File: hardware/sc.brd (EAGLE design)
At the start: 92 x 56 mm, 102 parts, among them K1 RT424F124, K2 RT424F124, Q1 si2305cd, Q2 8MHz, Q3 si2305cd, Q4 si2305cd, Q5 si2305cd, Q7 si2305cd, T1 BC846, T2 BC846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

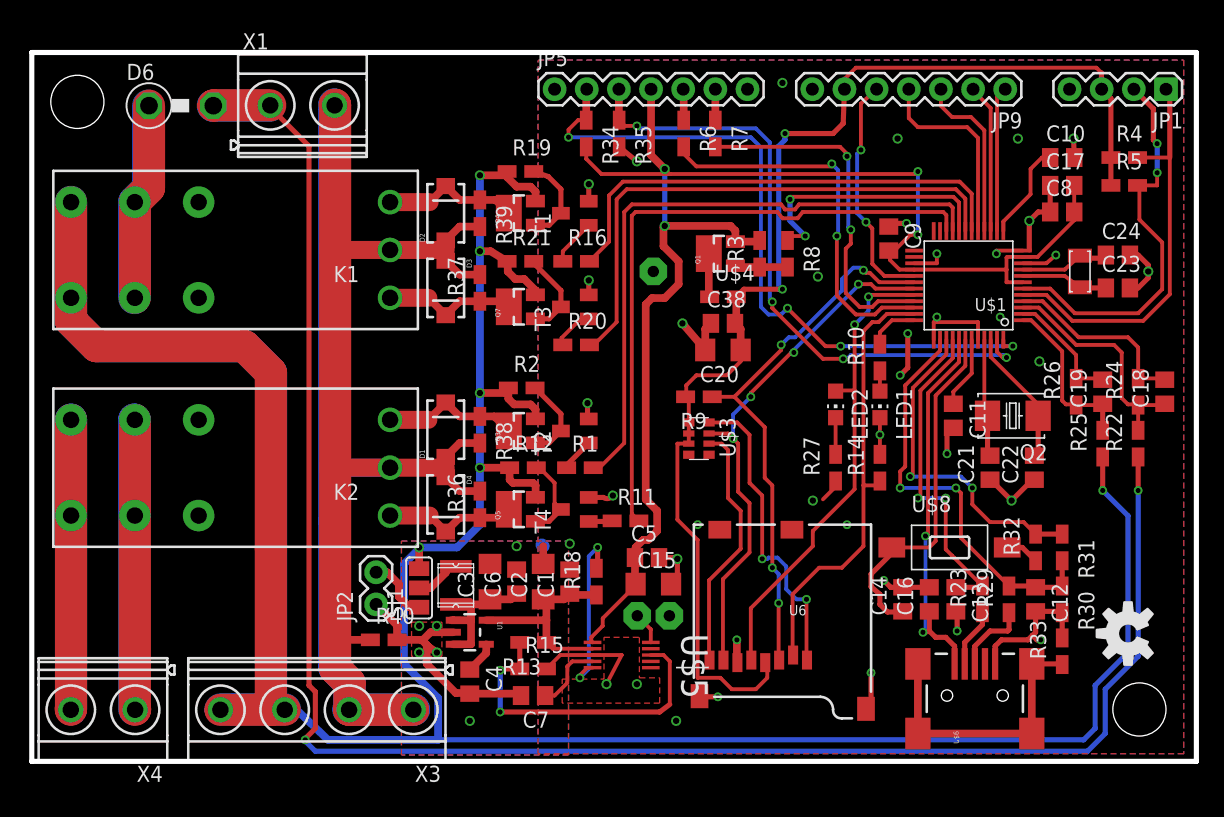
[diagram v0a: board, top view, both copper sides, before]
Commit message: calculate resistor dividers and XT1, XT2 load caps
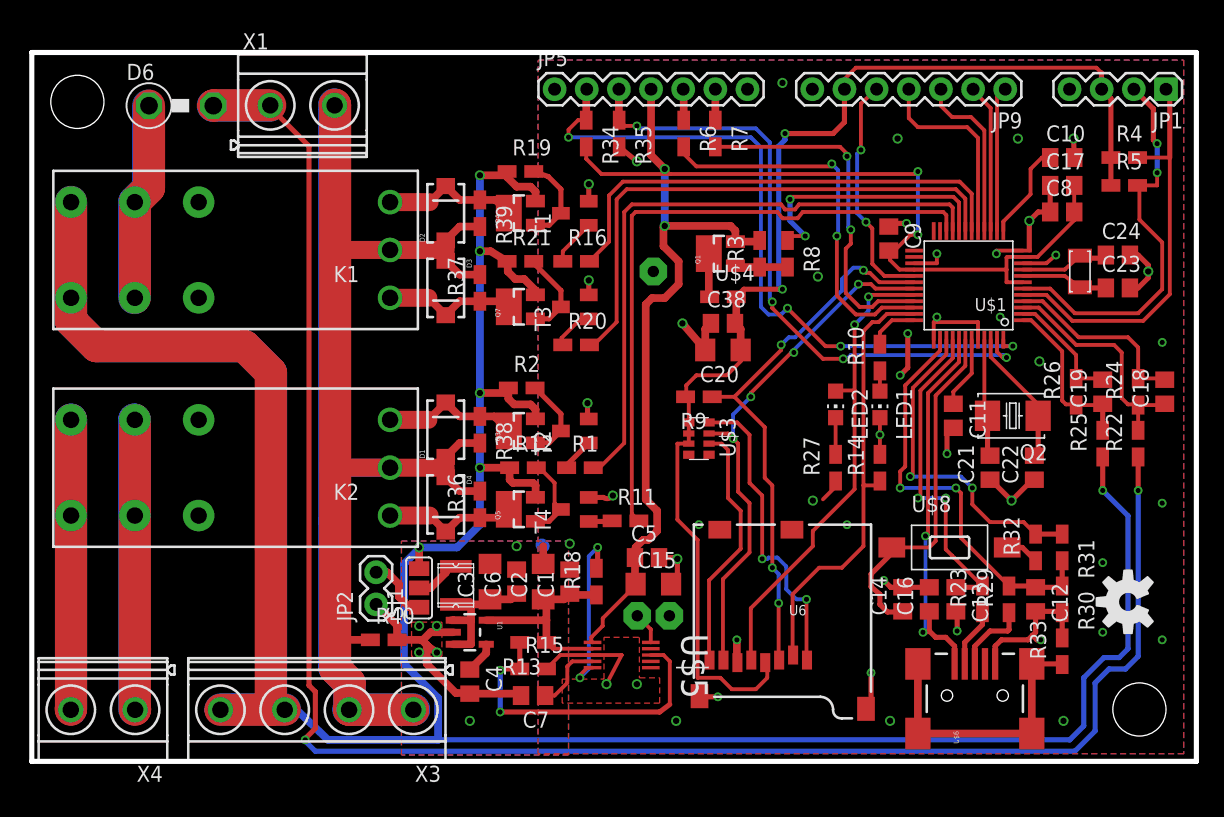
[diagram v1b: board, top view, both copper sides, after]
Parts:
- C13: value 10p -> 10pF
- C14: value 100n -> 100nF
- C18, C19: value 100nF -> 10nF
- C21, C22: value 22p -> 33pF
- C23, C24: value 22p -> 22pF
- C4: value 470pF -> 1uF
- LED2: value green -> orange
- Q2: value 8MHz -> 8MHz 18pF
- R15: value NA -> 56k
- R22, R25: value 100k -> 2M
- R24, R26: value 100k -> 240k
- Y1: value 32768Hz -> 32768Hz CFPX-217 12.5pF
- moved U$7 2.50 mm to (86.6, 12.6)
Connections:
- net VBAT_IN renamed PV+
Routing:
- net GND: vias 43 -> 52
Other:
- board text added: "+"
- board text added: "-"
- board text added: "1.0"
- board text added: "1.1"
- board text added: "1.2"
- board text added: "1.3"
- board text added: "12V bat"
- board text added: "4.0"
- board text added: "debug"
- board text added: "digital"
- board text added: "en"
- board text added: "gnd"
- board text added: "i2c"
- board text added: "opt sw"
- board text added: "photov"
- board text added: "pv+"
- board text added: "pv-"
- board text added: "rst"
- board text added: "rx"
- board text added: "test"
- board text added: "tx"
- board text added: "vcc"

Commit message: use different p-mosfet
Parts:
- Q3, Q4, Q5, Q7: value si2305cd -> IRLML9301
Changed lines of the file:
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@@
 <element name="R9" library="rcl" package="R0805W" value="10k" x="52.7" y="28.8" rot="R180"/>
 <element name="R14" library="rcl" package="R0805W" value="1M" x="67" y="23.2" rot="R90"/>
-<element name="Q4" library="Simplex-DiscreteSemi" package="SOT23-3_POWER" value="si2305cd" x="38.4" y="43.3" rot="R90"/>
+<element name="Q4" library="Simplex-DiscreteSemi" package="SOT23-3_POWER" value="IRLML9301" x="38.4" y="43.3" rot="R90"/>
 <element name="T1" library="transistor" package="SOT23" value="BC846" x="42.9" y="43.3" rot="R90"/>
 <element name="R16" library="rcl" package="R0805W" value="100k" x="43" y="39.5"/>
 <element name="R19" library="rcl" package="R0805W" value="10k" x="38.6" y="46.6"/>
-<element name="Q7" library="Simplex-DiscreteSemi" package="SOT23-3_POWER" value="si2305cd" x="38.4" y="35.9" rot="R90"/>
+<element name="Q7" library="Simplex-DiscreteSemi" package="SOT23-3_POWER" value="IRLML9301" x="38.4" y="35.9" rot="R90"/>
 <element name="T3" library="transistor" package="SOT23" value="BC846" x="42.9" y="35.9" rot="R90"/>
 <element name="R20" library="rcl" package="R0805W" value="100k" x="43" y="32.9"/>
@@
 <attribute name="OC_FARNELL" value="unknown" x="15.7" y="23.2" size="1.778" layer="27" rot="R180" display="off"/>
 </element>
-<element name="Q3" library="Simplex-DiscreteSemi" package="SOT23-3_POWER" value="si2305cd" x="38.4" y="26.1" rot="R90"/>
+<element name="Q3" library="Simplex-DiscreteSemi" package="SOT23-3_POWER" value="IRLML9301" x="38.4" y="26.1" rot="R90"/>
 <element name="T2" library="transistor" package="SOT23" value="BC846" x="42.9" y="26.1" rot="R90"/>
 <element name="R1" library="rcl" package="R0805W" value="100k" x="43.3" y="23.2"/>
 <element name="R2" library="rcl" package="R0805W" value="10k" x="38.7" y="29.5"/>
-<element name="Q5" library="Simplex-DiscreteSemi" package="SOT23-3_POWER" value="si2305cd" x="38.4" y="19.9" rot="R90"/>
+<element name="Q5" library="Simplex-DiscreteSemi" package="SOT23-3_POWER" value="IRLML9301" x="38.4" y="19.9" rot="R90"/>
 <element name="T4" library="transistor" package="SOT23" value="BC846" x="42.9" y="19.9" rot="R90"/>
 <element name="R11" library="rcl" package="R0805W" value="100k" x="46.9" y="19"/>

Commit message: rev3
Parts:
- removed D1, D3, D4: M4, SparkFun-DiscreteSemi:SMA-DIODE
- removed D6: diode, diode:C1702-05
- removed K1, K2: RT424F124, relay:RT424
- removed Q4, Q5, Q7: IRLML9301, Simplex-DiscreteSemi:SOT23-3_POWER
- removed R1: 100k, rcl:R0805W
- removed R37, R38, R39: 470, rcl:R0805W
- removed SJ1: pwr_sel, jumper:SJ_2
- removed T2, T3, T4: BC846, transistor:SOT23
- removed X1, X4: MKDSN1,5/2-5,08, con-phoenix-508:MKDSN1,5/2-5,08
- added C25, C28: 100nF, rcl:C0805
- added C26: 1uF, SparkFun-Capacitors:PANASONIC_D
- added C27: 10uF, SparkFun-Capacitors:PANASONIC_D
- added IC1: PB137ACV, linear:TO220V
- added IC2: INA168, burr-brown:SOT23-5
- added LED3, LED4, LED5, LED6, LED7, LED8: green, led:CHIP-LED0805
- added R17, R28: 1K, rcl:R0805W
- added RL: 150k, rcl:R0805W
- added RS: 0R05, Simplex-rlc:TO220ACS
- D2: value M4 -> SB560; device SparkFun-DiscreteSemi:SMA-DIODE -> diode:C1702-05
- JP2: value bat -> thermistor; device SparkFun:1X02 -> SparkFun-Connectors:1X02
- Q3: value IRLML9301 -> IRFR5305; device Simplex-DiscreteSemi:SOT23-3_POWER -> transistor-power:D-PAK_TO252AA
- R11: value 100k -> 30k
- R12, R21: value 10k -> 1K
- R20: value 100k -> 1K
- R36: value 470 -> 1K
- moved U$7 62.6 mm to (25.1, 24.2), turned to 0 degrees
- moved T1 46.6 mm to (5.30, 15.7), turned to 0 degrees
- moved R19 41.8 mm to (6.30, 20.0), turned to 270 degrees
- moved R2 35.8 mm to (4.20, 20.0), turned to 90 degrees
- moved Q3 33.3 mm to (5.20, 28.5), turned to 0 degrees
- moved JP2 25.8 mm to (1.80, 17.0), turned to 270 degrees
- moved R16 22.1 mm to (34.2, 19.2)
- moved D2 21.4 mm to (14.1, 32.7), turned to 180 degrees
- moved R36 18.7 mm to (34.2, 39.0), turned to 180 degrees
- moved R11 15.5 mm to (41.7, 4.40), turned to 270 degrees
- moved R20 14.5 mm to (34.2, 21.4)
- moved X3 12.1 mm to (10.5, 5.70)
- moved C22 10.0 mm to (70.1, 27.4), turned to 270 degrees
- moved C21 9.84 mm to (66.8, 27.4), turned to 270 degrees
- moved U$2 9.41 mm to (24.1, 14.3)
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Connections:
- removed net CHARGE_OFF: R20.2, U$1.19
- removed net CHARGE_ON: R16.2, U$1.18
- removed net N$31: R20.1, T3.1
- removed net N$32: Q7.1, R21.2, T3.3
- removed net N$33: K2.11, K2.21, X4.1
- removed net N$35: D3.C, K1.A2, Q7.3, R37.1
- removed net N$40: SJ1.2, U$2.P$1
- removed net N$8: R1.1, T2.1
- removed net P6.2: C18.1, R22.2, R24.1, U$1.3
- removed net P6.3: C18.2, R24.2, U$1.4
- removed net R_OFF: R11.2, U$1.22
- removed net R_ON: R1.2, U$1.21
- removed net VBAT_IN_D: D6.C, K1.11, K1.21
- new net N$24: LED8.A, R36.1
- new net P1.4: R12.2, U$1.18
- new net P1.5: R17.2, U$1.19
- new net P1.7: R20.2, U$1.21
- new net P2.0: R16.2, U$1.22
- new net P5.0: C25.1, JP2.2, R11.2, U$1.5
- new net P5.1: C28.2, IC2.1, RL.1, U$1.6
- new net SENSE: D2.A, Q3.4, R36.2
- net GND: now also C18.2, C19.2, C25.2, C28.1, LED3.C, LED4.C, LED5.C, R24.2, R26.2; no longer JP2.1, T1.2, T2.2, T3.2, T4.2
- net N$10: now also C26.+, IC1.1, IC2.4, IC2.5, RS.A; no longer Q3.1, R2.2, T2.3
- net N$12: now also LED6.A, R21.1; no longer D1.C, K2.A1, Q3.3, R38.1
- net N$15: now also LED4.A, R17.1; no longer R11.1, T4.1
- net N$16: now also LED5.A, R20.1; no longer Q5.1, R12.2, T4.3
- net N$18: now also LED7.A, R28.1; no longer D4.C, K2.A2, Q5.3, R36.1
- net N$28: now also Q3.1, R2.2; no longer Q4.1, R19.2, T1.3
- net N$30: now also IC2.3, RS.C; no longer K1.A1, Q4.3, R39.1
- net N$5: now also R19.2, R2.1, T1.3; no longer K2.14, K2.24, X4.2
- net N$9: now also LED3.A, R12.1; no longer JP2.2, SJ1.1
- net P6.1: now also C18.1, R22.2, R24.1; no longer C19.2, R26.2
- net PV+: now also Q3.3, R19.1, R21.2, X3.4; no longer D6.A, X1.1
- net SCL: now also U$1.3; no longer U$1.5
- net SDA: now also U$1.4; no longer U$1.6
- net VBAT: now also C27.+, IC1.3, R28.2, U$2.P$1; no longer K1.14, K1.24, Q3.2, Q4.2, Q5.2, Q7.2, R12.1, R19.1, R2.1, R21.1, SJ1.3, X3.4
- net VBAT_GND: now also C26.-, C27.-, IC1.2, IC2.2, JP2.1, LED6.C, LED7.C, LED8.C, RL.2, T1.2; no longer D1.A, D2.A, D3.A, D4.A, K1.A3, K2.A3, R36.2, R37.2, R38.2, R39.2, X1.2
- net VCC_EN: now also R11.1
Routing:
- net P5.1: track 0.00 -> 158.8 mm, vias 0 -> 5
- net P5.0: track 0.00 -> 130.5 mm, vias 0 -> 3
- net VBAT_GND: track 157.9 -> 48.8 mm, vias 0 -> 13
- net VBAT: track 284.6 -> 213.0 mm, vias 6 -> 3
- net N$33: track 53.4 -> 0.00 mm
- net P2.0: track 0.00 -> 53.3 mm
- net P1.7: track 0.00 -> 52.7 mm
- net R_OFF: track 51.1 -> 0.00 mm
- net P1.5: track 0.00 -> 51.0 mm
- net R_ON: track 50.7 -> 0.00 mm
- net P1.4: track 0.00 -> 48.0 mm
- net CHARGE_OFF: track 43.3 -> 0.00 mm
- net N$5: track 45.8 -> 4.66 mm
- net VBAT_IN_D: track 38.5 -> 0.00 mm
- net CHARGE_ON: track 38.3 -> 0.00 mm
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- added copper zone on layer 1, net VBAT_GND
- added copper zone on layer 16, net VBAT_GND
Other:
- board size 92 x 56 mm -> 82.8 x 56 mm
- board text added: "12v bat"
- board text added: "15-36v pv cell"
- board text added: "bat"
- board text added: "chg"
- board text added: "pv"
- board text added: "s0"
- board text added: "s1"
- board text added: "s2"
- board text added: "sc rev 03 Petre Rodan 201308"
- board text added: "th"
- board text removed: "+"
- board text removed: "-"
- board text removed: "12V bat"
- board text removed: "opt sw"
- board text removed: "photov"
- board text removed: "pv+"
- board text removed: "pv-"
- board text removed: "sc rev 01 Petre Rodan 201305"

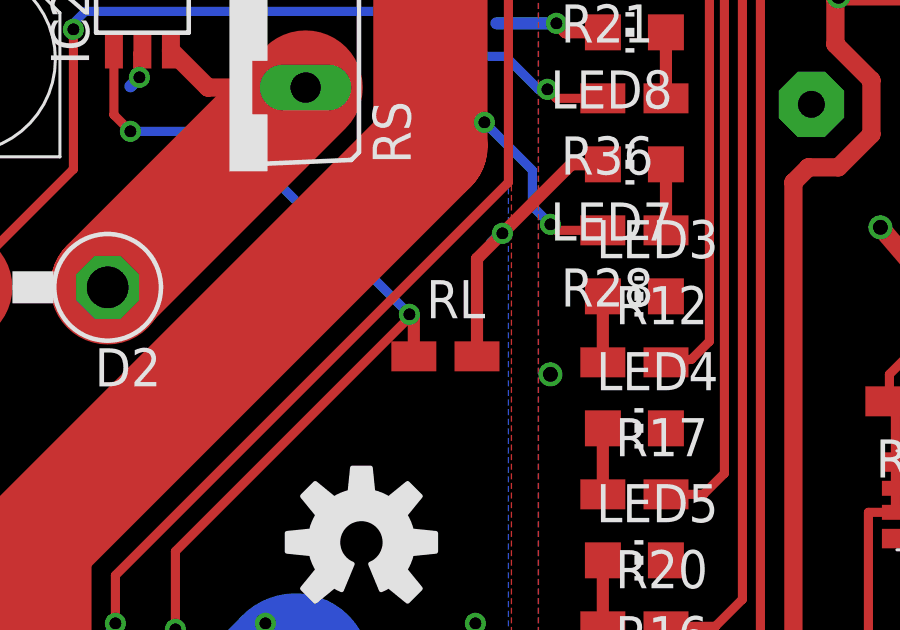
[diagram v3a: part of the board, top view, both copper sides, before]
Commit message: review part values
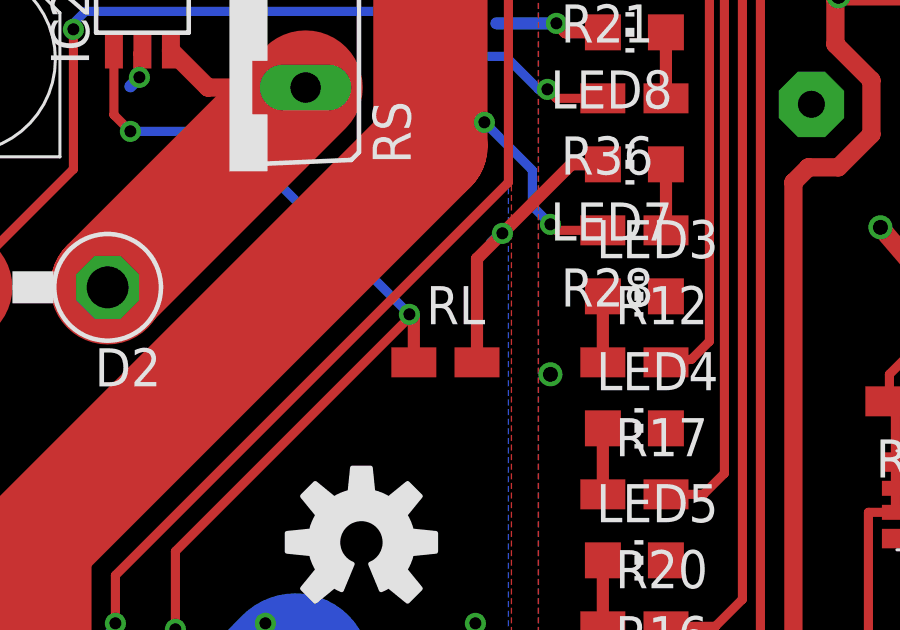
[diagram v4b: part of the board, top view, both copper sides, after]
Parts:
- C18, C19: value 10nF -> 100nF
- R21, R28, R36: value 1K -> 220k
- R26: value 240k -> 470k
- moved RL 0.20 mm to (27.9, 30.2)
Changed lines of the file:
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@@
 <element name="R24" library="rcl" package="R0805W" value="240k" x="78.4" y="29.3" rot="R90"/>
 <element name="R25" library="rcl" package="R0805W" value="2M" x="75.6" y="25.2" rot="R90"/>
-<element name="R26" library="rcl" package="R0805W" value="240k" x="73.5" y="29.3" rot="R90"/>
+<element name="R26" library="rcl" package="R0805W" value="470k" x="73.5" y="29.3" rot="R90"/>
 <element name="R3" library="rcl" package="R0805W" value="100k" x="48.5" y="40.2" rot="R90"/>
 <element name="Q1" library="Simplex-DiscreteSemi" package="SOT23-3_POWER" value="si2305cd" x="45.2" y="40.2" rot="R90"/>
@@
 <element name="C15" library="rcl" package="C1206" value="10uF" x="40.1" y="14.1"/>
 <element name="U$8" library="Simplex-Switches" package="6X3.5_TACTILE_SW" value="USB_BSL" x="63.5" y="17"/>
-<element name="C18" library="rcl" package="C0805" value="10nF" x="80.5" y="29.3" rot="R90"/>
-<element name="C19" library="rcl" package="C0805" value="10nF" x="75.6" y="29.3" rot="R90"/>
+<element name="C18" library="rcl" package="C0805" value="100nF" x="80.5" y="29.3" rot="R90"/>
+<element name="C19" library="rcl" package="C0805" value="100nF" x="75.6" y="29.3" rot="R90"/>
 <element name="JP1" library="SparkFun-Connectors" package="1X04" value="i2c" x="80.6" y="53.2" rot="R180"/>
 <element name="X3" library="con-phoenix-508" package="MKDSN1,5/4-5,08" value="MKDSN1,5/4-5,08" x="10.5" y="5.7" rot="R180">
@@
 <element name="R20" library="rcl" package="R0805W" value="1K" x="34.2" y="21.4"/>
 <element name="LED5" library="led" package="CHIP-LED0805" value="green" x="34.2" y="23.6" rot="R270"/>
-<element name="R21" library="rcl" package="R0805W" value="1K" x="34.2" y="43.4" rot="R180"/>
+<element name="R21" library="rcl" package="R0805W" value="220k" x="34.2" y="43.4" rot="R180"/>
 <element name="LED6" library="led" package="CHIP-LED0805" value="green" x="34.2" y="45.6" rot="R90"/>
-<element name="R28" library="rcl" package="R0805W" value="1K" x="34.2" y="34.6" rot="R180"/>
+<element name="R28" library="rcl" package="R0805W" value="220k" x="34.2" y="34.6" rot="R180"/>
 <element name="LED7" library="led" package="CHIP-LED0805" value="green" x="34.2" y="36.8" rot="R90"/>
-<element name="R36" library="rcl" package="R0805W" value="1K" x="34.2" y="39" rot="R180"/>
+<element name="R36" library="rcl" package="R0805W" value="220k" x="34.2" y="39" rot="R180"/>
 <element name="LED8" library="led" package="CHIP-LED0805" value="green" x="34.2" y="41.2" rot="R90"/>
 <element name="D2" library="diode" package="C1702-05" value="SB560" x="14.1" y="32.7" rot="R180"/>
-<element name="RL" library="rcl" package="R0805W" value="150k" x="27.9" y="30.4"/>
+<element name="RL" library="rcl" package="R0805W" value="150k" x="27.9" y="30.2"/>
 <element name="C28" library="rcl" package="C0805" value="100nF" x="75" y="12.9" rot="R270"/>
 </elements>
@@
 <wire x1="18.1" y1="15.1" x2="22.9" y2="20" width="5" layer="16"/>
 <contactref element="RL" pad="2"/>
-<wire x1="28.9525" y1="30.4" x2="28.9525" y2="33.6525" width="0.4064" layer="1"/>
+<wire x1="28.9525" y1="30.2" x2="28.9525" y2="33.6525" width="0.4064" layer="1"/>
 <wire x1="28.9525" y1="33.6525" x2="29.8" y2="34.5" width="0.4064" layer="1"/>
 <polygon width="0.254" layer="1" isolate="0.3048" thermals="no">
@@
 <contactref element="RL" pad="1"/>
 <wire x1="26.7" y1="31.7" x2="26.8475" y2="31.7" width="0.4064" layer="1"/>
-<wire x1="26.8475" y1="31.7" x2="26.8475" y2="30.4" width="0.4064" layer="1"/>
+<wire x1="26.8475" y1="31.7" x2="26.8475" y2="30.2" width="0.4064" layer="1"/>
 <contactref element="C28" pad="2"/>
 <wire x1="75" y1="11.95" x2="75" y2="10.8" width="0.4064" layer="1"/>

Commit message: resistor tweaks
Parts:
- R10: value 1K -> 2k2
- R24: value 240k -> 220k
- R26: value 470k -> 330k
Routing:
- net VBAT_GND: track 49.0 -> 49.7 mm, vias 13 -> 17
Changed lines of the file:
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@@
 <element name="R19" library="rcl" package="R0805W" value="10k" x="6.3" y="20" rot="R270"/>
 <element name="R22" library="rcl" package="R0805W" value="2M" x="78.4" y="25.2" rot="R90"/>
-<element name="R24" library="rcl" package="R0805W" value="240k" x="78.4" y="29.3" rot="R90"/>
+<element name="R24" library="rcl" package="R0805W" value="220k" x="78.4" y="29.3" rot="R90"/>
 <element name="R25" library="rcl" package="R0805W" value="2M" x="75.6" y="25.2" rot="R90"/>
-<element name="R26" library="rcl" package="R0805W" value="470k" x="73.5" y="29.3" rot="R90"/>
+<element name="R26" library="rcl" package="R0805W" value="330k" x="73.5" y="29.3" rot="R90"/>
 <element name="R3" library="rcl" package="R0805W" value="100k" x="48.5" y="40.2" rot="R90"/>
 <element name="Q1" library="Simplex-DiscreteSemi" package="SOT23-3_POWER" value="si2305cd" x="45.2" y="40.2" rot="R90"/>
 <element name="R8" library="rcl" package="R0805W" value="10k" x="50.7" y="40.2" rot="R270"/>
 <element name="LED1" library="led" package="CHIP-LED0805" value="green" x="58" y="28.3" rot="R180"/>
-<element name="R10" library="rcl" package="R0805W" value="1K" x="58" y="32" rot="R90"/>
+<element name="R10" library="rcl" package="R0805W" value="2k2" x="58" y="32" rot="R90"/>
 <element name="U$5" library="Simplex-ICs" package="MSOP_10P" value="TPS3613" x="35.3" y="9.5" rot="R270"/>
 <element name="R13" library="rcl" package="R0805W" value="100k" x="30.6" y="9.5" rot="R180"/>
@@
 <wire x1="6.1" y1="13.1" x2="5.9" y2="13.1" width="0.4064" layer="16"/>
 <wire x1="17.8" y1="40.594" x2="17.7" y2="40.494" width="0.4064" layer="1"/>
-<wire x1="17.7" y1="40.494" x2="17.7" y2="39.7" width="0.4064" layer="1"/>
-<via x="17.7" y="39.7" extent="1-16" drill="0.4"/>
-<wire x1="17.7" y1="39.7" x2="17.4" y2="39.4" width="0.4064" layer="16"/>
+<wire x1="17.7" y1="40.494" x2="18" y2="39.2" width="0.4064" layer="1"/>
+<via x="18" y="39.2" extent="1-16" drill="0.4"/>
+<wire x1="18" y1="39.2" x2="17.4" y2="39.4" width="0.4064" layer="16"/>
 <contactref element="C27" pad="-"/>
 <contactref element="C26" pad="-"/>
@@
 <via x="12.6" y="28.3" extent="1-16" drill="0.4"/>
 <via x="18.1" y="15.7" extent="1-16" drill="0.4"/>
+<via x="15.9" y="52.4" extent="1-16" drill="0.4"/>
+<via x="7.7" y="52.4" extent="1-16" drill="0.4"/>
+<via x="9.8" y="36.5" extent="1-16" drill="0.4"/>
+<via x="12.6" y="36.5" extent="1-16" drill="0.4"/>
 </signal>
 <signal name="PV+">

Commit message: resistor value tweaks
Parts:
- RL: value 150k -> 110k
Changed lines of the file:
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@@
 <element name="LED8" library="led" package="CHIP-LED0805" value="green" x="34.2" y="41.2" rot="R90"/>
 <element name="D2" library="diode" package="C1702-05" value="SB560" x="14.1" y="32.7" rot="R180"/>
-<element name="RL" library="rcl" package="R0805W" value="150k" x="27.9" y="30.2"/>
+<element name="RL" library="rcl" package="R0805W" value="110k" x="27.9" y="30.2"/>
 <element name="C28" library="rcl" package="C0805" value="100nF" x="75" y="12.9" rot="R270"/>
 </elements>
